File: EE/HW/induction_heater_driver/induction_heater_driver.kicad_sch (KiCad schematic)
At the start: 0 parts

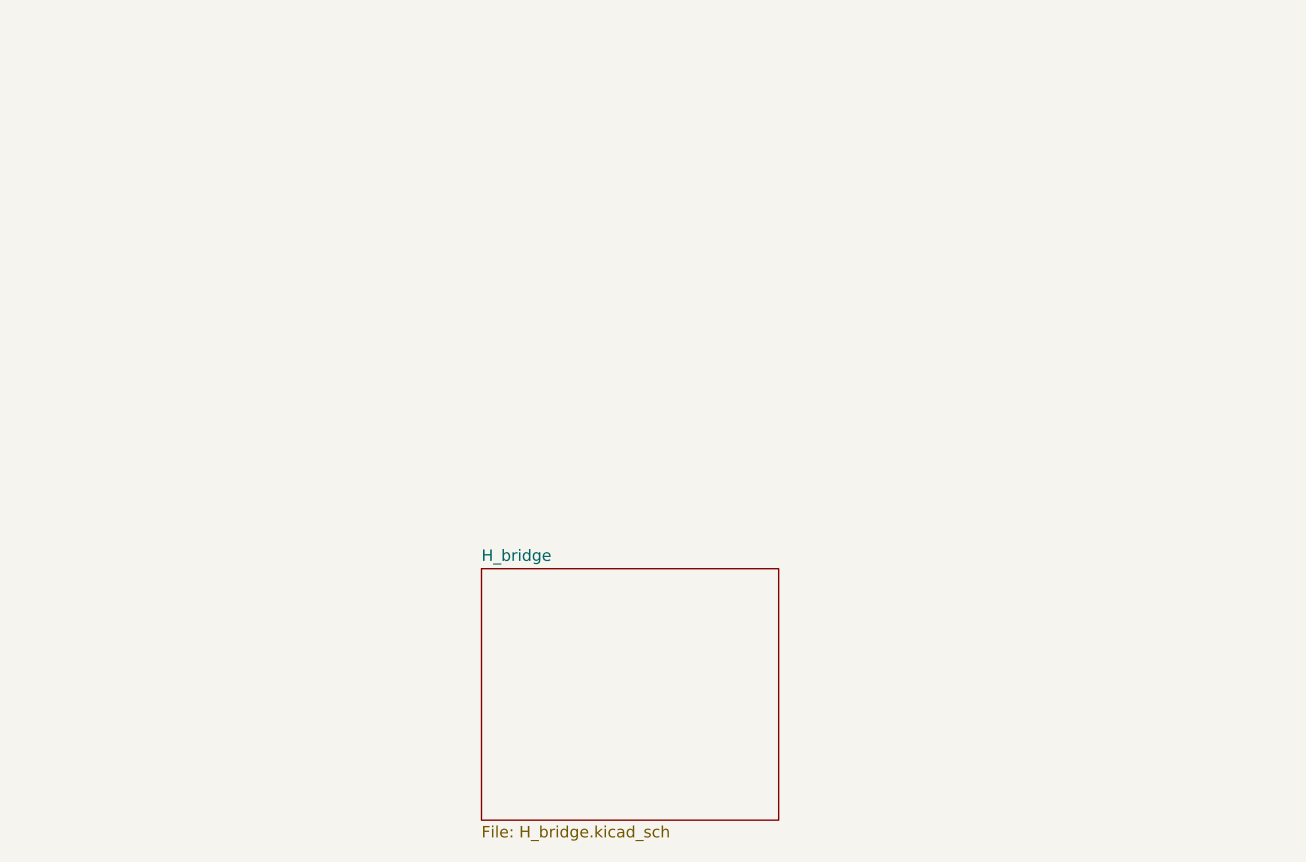
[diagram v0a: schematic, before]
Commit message: imported MAG package from github
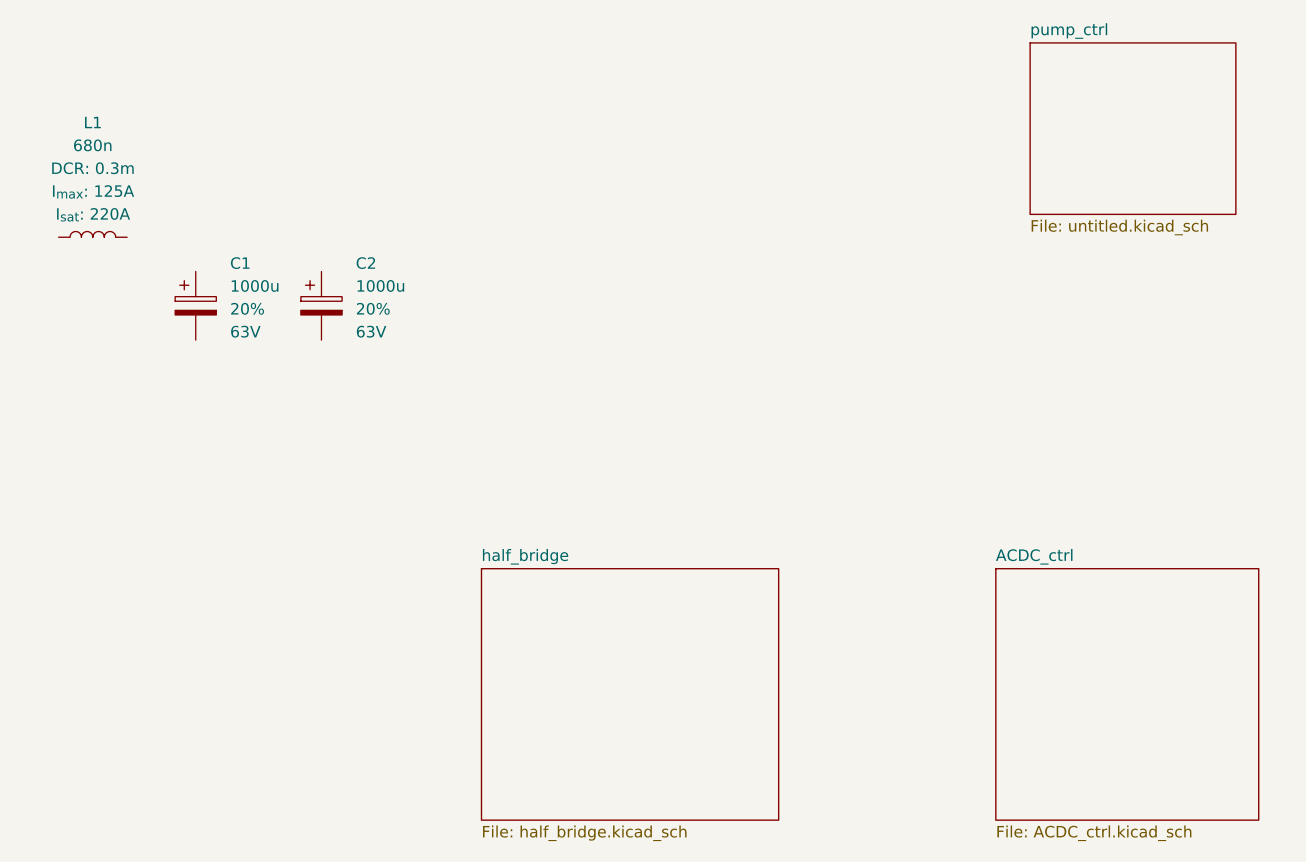
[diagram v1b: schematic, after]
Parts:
- added C1, C2: 1000u, peml:CP_Radial_D16.0mm_P7.50mm, symbol peml_passives:63YXJ1000M16X25
- added L1: 680n, peml:IHDM1107BBEVR68M30, symbol peml_passives:IHDM1107BBEVR68M30
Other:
- sheet H_bridge renamed half_bridge
- added sheet ACDC_ctrl (ACDC_ctrl.kicad_sch)
- added sheet pump_ctrl (untitled.kicad_sch)
- sheet half_bridge: file H_bridge.kicad_sch -> half_bridge.kicad_sch
